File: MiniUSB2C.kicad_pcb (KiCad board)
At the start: 2 copper layers, 11.2 x 11.3 mm, 3 parts, among them J1 USB

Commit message: smaller
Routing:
- net GNDPWR: track 6.61 -> 15.6 mm
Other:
- board size 11.2 x 11.3 mm -> 9.7 x 11.2 mm

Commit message: smaller smaller
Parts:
- moved LOGO4 1.40 mm to (44.3, 43.8)
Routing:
- net /USB_D+: track 8.07 -> 7.38 mm
- net /USB_D-: track 6.05 -> 5.40 mm
- net VBUS: track 10.1 -> 9.49 mm
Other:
- board size 9.7 x 11.2 mm -> 9.7 x 9.3 mm
- net class Default: clearance 0.2 -> 0.16
- rule trace_clearance: 0.2 -> 0.16
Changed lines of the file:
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@@
     (links 16)
     (no_connects 0)
-    (area 39.421999 39.548999 49.224001 50.875001)
+    (area 39.421999 41.453999 49.224001 50.875001)
     (thickness 1.2)
-    (drawings 12)
-    (tracks 40)
+    (drawings 8)
+    (tracks 45)
     (zones 0)
     (modules 3)
@@
     (last_trace_width 0.381)
     (user_trace_width 0.381)
-    (trace_clearance 0.2)
+    (trace_clearance 0.16)
     (zone_clearance 0.308)
     (zone_45_only no)
@@
   (net 9 VBUS)
   (net_class Default 这是默认网络组.
-    (clearance 0.2)
+    (clearance 0.16)
     (trace_width 0.25)
     (via_dia 0.6)
@@
   )
   (module ktec:KTEC_Logo (layer B.Cu)
-    (at 44.323 42.418 180)
+    (at 44.323 43.815 180)
     (fp_text reference LOGO4 (at 0 2.8575 180) (layer B.SilkS) hide
       (effects (font (size 1.016 1.016) (thickness 0.1524)) (justify mirror))
@@
       (xy -0.004174 2.092787)) (layer B.Mask) (width 0.01))
   )
+  (dimension 9.271 (width 0.3) (layer Eco1.User)
+    (gr_text "9.271 mm" (at 30.781 46.1645 270) (layer Eco1.User)
+      (effects (font (size 1.5 1.5) (thickness 0.3)))
+    )
+    (feature1 (pts (xy 39.497 50.8) (xy 29.431 50.8)))
+    (feature2 (pts (xy 39.497 41.529) (xy 29.431 41.529)))
+    (crossbar (pts (xy 32.131 41.529) (xy 32.131 50.8)))
+    (arrow1a (pts (xy 32.131 50.8) (xy 31.544579 49.673496)))
+    (arrow1b (pts (xy 32.131 50.8) (xy 32.717421 49.673496)))
+    (arrow2a (pts (xy 32.131 41.529) (xy 31.544579 42.655504)))
+    (arrow2b (pts (xy 32.131 41.529) (xy 32.717421 42.655504)))
+  )
+  (gr_line (start 49.149 41.529) (end 39.497 41.529) (angle 90) (layer Edge.Cuts) (width 0.15))
   (dimension 9.652 (width 0.3) (layer Eco1.User)
     (gr_text "9.652 mm" (at 44.323 28.749) (layer Eco1.User)
@@
     (arrow2b (pts (xy 39.497 30.099) (xy 40.623504 29.512579)))
   )
-  (dimension 11.176 (width 0.3) (layer Eco1.User)
-    (gr_text "11.176 mm" (at 34.972 45.212 270) (layer Eco1.User)
-      (effects (font (size 1.5 1.5) (thickness 0.3)))
-    )
-    (feature1 (pts (xy 39.878 50.8) (xy 33.622 50.8)))
-    (feature2 (pts (xy 39.878 39.624) (xy 33.622 39.624)))
-    (crossbar (pts (xy 36.322 39.624) (xy 36.322 50.8)))
-    (arrow1a (pts (xy 36.322 50.8) (xy 35.735579 49.673496)))
-    (arrow1b (pts (xy 36.322 50.8) (xy 36.908421 49.673496)))
-    (arrow2a (pts (xy 36.322 39.624) (xy 35.735579 40.750504)))
-    (arrow2b (pts (xy 36.322 39.624) (xy 36.908421 40.750504)))
-  )
-  (gr_line (start 40.64 41.275) (end 39.497 41.275) (angle 90) (layer Edge.Cuts) (width 0.15))
   (gr_line (start 46.99 50.8) (end 41.656 50.8) (angle 90) (layer Edge.Cuts) (width 0.15))
   (gr_line (start 49.149 48.641) (end 46.99 50.8) (angle 90) (layer Edge.Cuts) (width 0.15))
-  (gr_line (start 49.149 41.275) (end 49.149 48.641) (angle 90) (layer Edge.Cuts) (width 0.15))
-  (gr_line (start 48.26 41.275) (end 49.149 41.275) (angle 90) (layer Edge.Cuts) (width 0.15))
-  (gr_line (start 48.26 39.624) (end 48.26 41.275) (angle 90) (layer Edge.Cuts) (width 0.15))
-  (gr_line (start 40.64 39.624) (end 48.26 39.624) (angle 90) (layer Edge.Cuts) (width 0.15))
+  (gr_line (start 49.149 41.529) (end 49.149 48.641) (angle 90) (layer Edge.Cuts) (width 0.15))
   (gr_line (start 39.497 48.641) (end 41.656 50.8) (angle 90) (layer Edge.Cuts) (width 0.15))
-  (gr_line (start 39.497 41.275) (end 39.497 48.641) (angle 90) (layer Edge.Cuts) (width 0.15))
-  (gr_line (start 40.64 39.624) (end 40.64 41.275) (angle 90) (layer Edge.Cuts) (width 0.15))
-  (segment (start 43.573 47.119) (end 43.573 46.089) (width 0.25) (layer F.Cu) (net 6))
-  (segment (start 44.45 46.228) (end 44.45 49.54778) (width 0.25) (layer B.Cu) (net 6))
-  (segment (start 43.942 45.72) (end 44.45 46.228) (width 0.25) (layer B.Cu) (net 6))
-  (via (at 43.942 45.72) (size 0.6) (drill 0.4) (layers F.Cu B.Cu) (net 6))
-  (segment (start 43.573 46.089) (end 43.942 45.72) (width 0.25) (layer F.Cu) (net 6))
+  (gr_line (start 39.497 41.529) (end 39.497 48.641) (angle 90) (layer Edge.Cuts) (width 0.15))
+  (segment (start 44.069 46.228) (end 43.561 46.228) (width 0.25) (layer B.Cu) (net 6))
+  (segment (start 44.45 46.863) (end 44.45 49.54778) (width 0.25) (layer B.Cu) (net 6))
+  (segment (start 44.45 46.609) (end 44.069 46.228) (width 0.25) (layer B.Cu) (net 6))
+  (segment (start 43.573 46.216) (end 43.573 46.597) (width 0.25) (layer F.Cu) (net 6))
+  (segment (start 43.573 46.609) (end 43.573 47.119) (width 0.25) (layer F.Cu) (net 6))
+  (segment (start 44.45 46.863) (end 44.45 46.609) (width 0.25) (layer B.Cu) (net 6))
+  (via (at 43.561 46.228) (size 0.6) (drill 0.4) (layers F.Cu B.Cu) (net 6))
+  (segment (start 43.561 46.228) (end 43.573 46.228) (width 0.25) (layer F.Cu) (net 6))
+  (segment (start 43.573 46.228) (end 43.573 46.216) (width 0.25) (layer F.Cu) (net 6))
   (segment (start 44.573 47.119) (end 44.573 47.883) (width 0.25) (layer F.Cu) (net 6))
   (segment (start 44.45 48.006) (end 44.45 49.54778) (width 0.25) (layer F.Cu) (net 6))
   (segment (start 44.573 47.883) (end 44.45 48.006) (width 0.25) (layer F.Cu) (net 6))
-  (segment (start 44.073 47.119) (end 44.073 46.478) (width 0.25) (layer F.Cu) (net 7))
-  (segment (start 45.085 45.974) (end 45.085 48.18634) (width 0.25) (layer B.Cu) (net 7))
-  (segment (start 44.831 45.72) (end 45.085 45.974) (width 0.25) (layer B.Cu) (net 7))
-  (via (at 44.831 45.72) (size 0.6) (drill 0.4) (layers F.Cu B.Cu) (net 7))
-  (segment (start 44.073 46.478) (end 44.831 45.72) (width 0.25) (layer F.Cu) (net 7))
+  (segment (start 44.45 46.228) (end 45.085 46.228) (width 0.25) (layer F.Cu) (net 7))
+  (segment (start 45.085 46.228) (end 45.085 46.863) (width 0.25) (layer B.Cu) (net 7))
+  (via (at 45.085 46.228) (size 0.6) (drill 0.4) (layers F.Cu B.Cu) (net 7))
+  (segment (start 44.073 47.119) (end 44.073 46.605) (width 0.25) (layer F.Cu) (net 7))
+  (segment (start 44.073 46.605) (end 44.45 46.228) (width 0.25) (layer F.Cu) (net 7))
+  (segment (start 45.085 46.863) (end 45.085 48.18634) (width 0.25) (layer B.Cu) (net 7))
   (segment (start 45.085 48.18634) (end 45.24756 48.3489) (width 0.25) (layer B.Cu) (net 7))
   (segment (start 45.085 48.18634) (end 45.24756 48.3489) (width 0.25) (layer B.Cu) (net 7))
@@
   (segment (start 39.998 46.404) (end 39.998 44.584) (width 0.381) (layer B.Cu) (net 8))
   (segment (start 39.998 44.584) (end 40.894 43.688) (width 0.381) (layer B.Cu) (net 8))
+  (segment (start 43.053 45.466) (end 45.593 45.466) (width 0.381) (layer F.Cu) (net 9))
+  (segment (start 41.923 47.119) (end 41.923 46.596) (width 0.381) (layer F.Cu) (net 9))
+  (segment (start 46.723 46.596) (end 46.723 47.119) (width 0.381) (layer F.Cu) (net 9))
+  (segment (start 45.593 45.466) (end 46.723 46.596) (width 0.381) (layer F.Cu) (net 9))
+  (segment (start 41.923 46.596) (end 43.053 45.466) (width 0.381) (layer F.Cu) (net 9))
   (segment (start 46.723 47.119) (end 46.723 48.87244) (width 0.381) (layer F.Cu) (net 9))
   (segment (start 46.723 48.87244) (end 46.04766 49.54778) (width 0.381) (layer F.Cu) (net 9))
-  (segment (start 41.923 47.119) (end 41.923 46.469) (width 0.381) (layer F.Cu) (net 9))
-  (segment (start 46.723 46.469) (end 46.723 47.119) (width 0.381) (layer F.Cu) (net 9))
-  (segment (start 45.212 44.958) (end 46.723 46.469) (width 0.381) (layer F.Cu) (net 9))
-  (segment (start 43.434 44.958) (end 45.212 44.958) (width 0.381) (layer F.Cu) (net 9))
-  (segment (start 41.923 46.469) (end 43.434 44.958) (width 0.381) (layer F.Cu) (net 9))
   (zone (net 8) (net_name GNDPWR) (layer F.Cu) (hatch edge 0.508)
     (connect_pads (clearance 0.308))
@@
     (polygon
       (pts
-        (xy 48.26 41.275) (xy 49.149 41.275) (xy 49.149 48.641) (xy 46.99 50.8) (xy 41.656 50.8)
-        (xy 39.497 48.641) (xy 39.497 41.275) (xy 40.64 41.275) (xy 40.64 39.624) (xy 48.26 39.624)
+        (xy 49.149 48.641) (xy 46.99 50.8) (xy 41.656 50.8) (xy 39.497 48.641) (xy 39.497 41.529)
+        (xy 49.149 41.529)
       )
     )
@@
     (polygon
       (pts
-        (xy 48.26 41.275) (xy 49.149 41.275) (xy 49.149 48.641) (xy 46.99 50.8) (xy 41.656 50.8)
-        (xy 39.497 48.641) (xy 39.497 41.275) (xy 40.64 41.275) (xy 40.64 39.624) (xy 48.26 39.624)
+        (xy 49.149 48.641) (xy 46.99 50.8) (xy 41.656 50.8) (xy 39.497 48.641) (xy 39.497 41.529)
+        (xy 49.149 41.529)
       )
     )

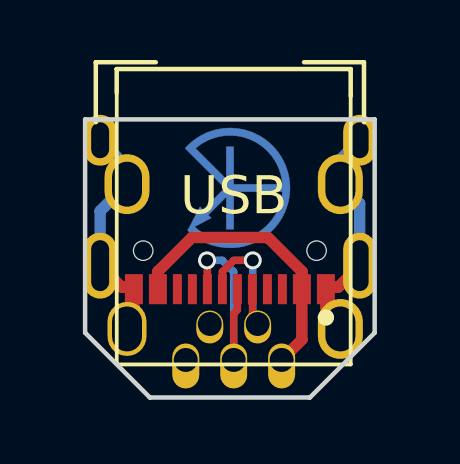
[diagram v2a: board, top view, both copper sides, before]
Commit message: v3: add 5.1K for CC pin
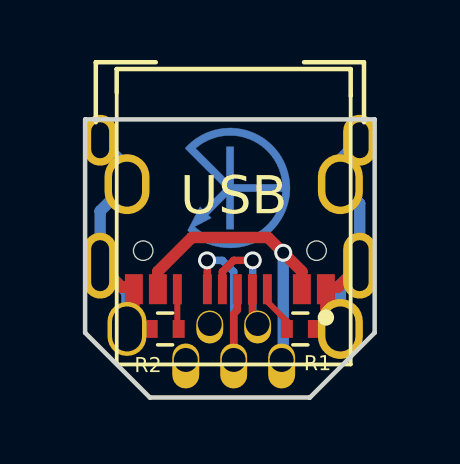
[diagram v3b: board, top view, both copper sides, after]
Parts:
- added R1: 5k1, Resistors_SMD:R_0402, F.Cu at (46.7, 48.5)
- added R2: 5k1, Resistors_SMD:R_0402, F.Cu at (42.2, 48.5)
- USB1: footprint YD_modules:USB_TYPE-C_16PIN -> YD_modules:USB_TYPE-C_16PIN2
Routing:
- net GNDPWR: track 15.6 -> 22.1 mm
- net Net-(R1-Pad1): track 0.00 -> 1.66 mm
- net Net-(R2-Pad1): track 0.00 -> 1.41 mm
- net VBUS: track 9.49 -> 10.6 mm, vias 0 -> 1
